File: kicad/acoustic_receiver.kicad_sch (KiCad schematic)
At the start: 17 parts, among them J1 JLI P48 High Z Buffer, J2 Inline Phantom Power 48V, U1 OPA2134, U2 OPA2134, U3 MCP3008

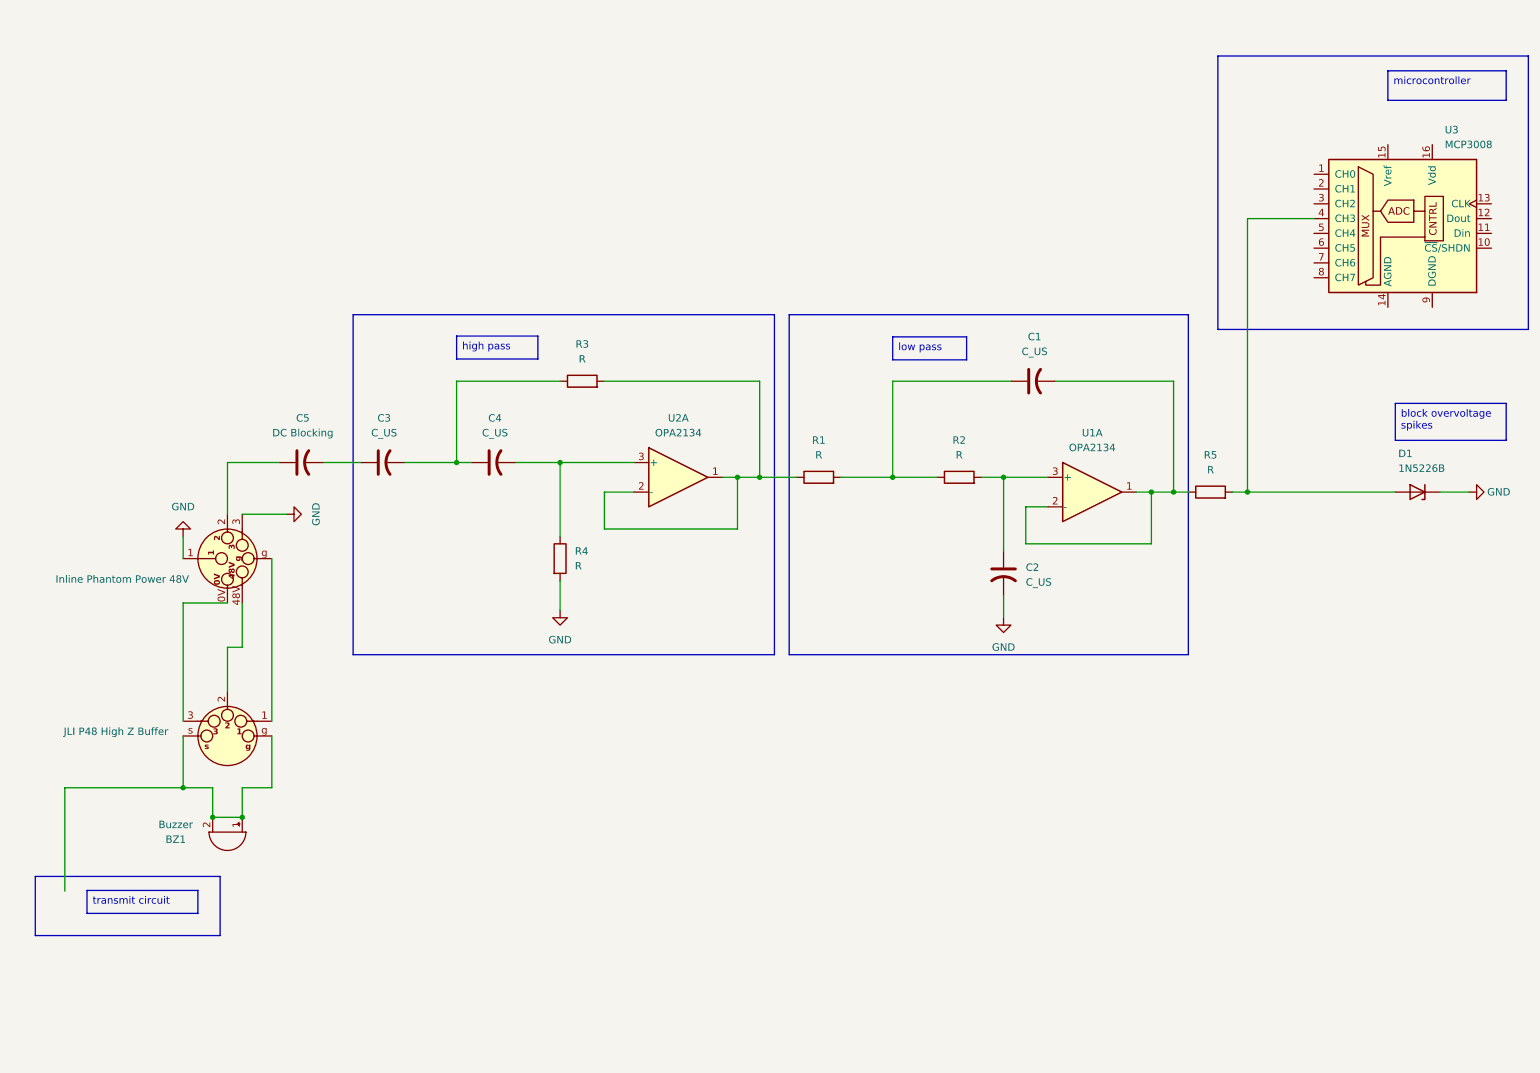
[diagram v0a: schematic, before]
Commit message: update modem diagrams
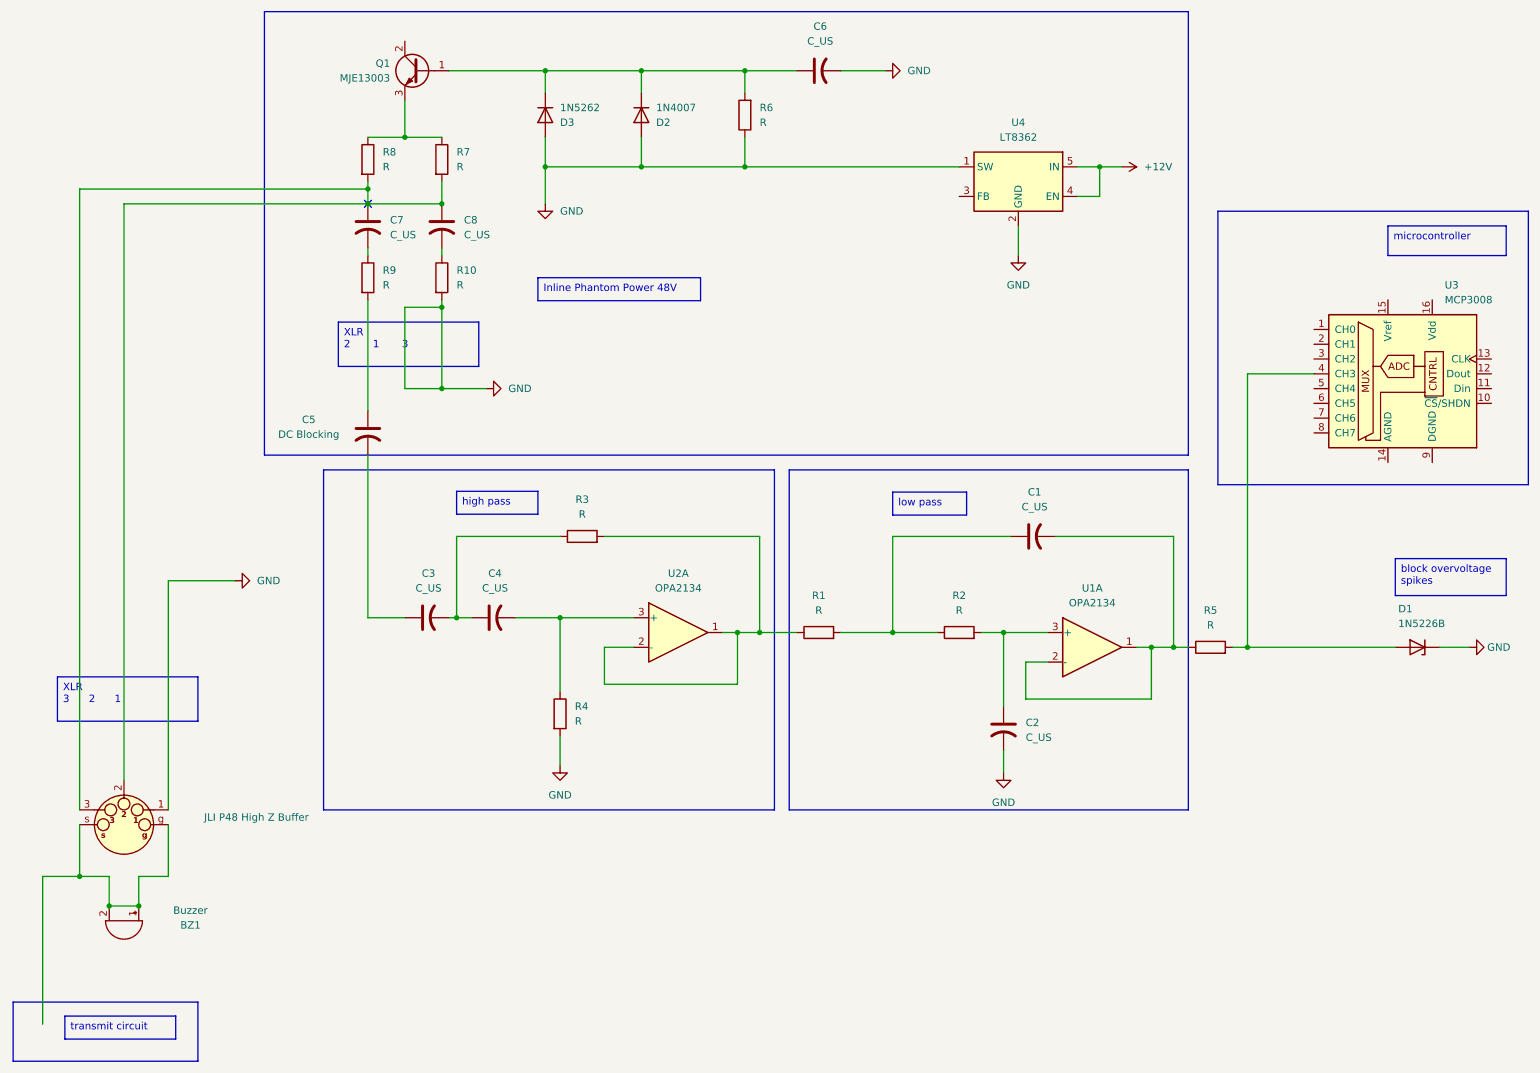
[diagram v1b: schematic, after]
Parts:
- removed J2: Inline Phantom Power 48V, symbol Connector_Audio:XLR6
- added C6, C7, C8: C_US, symbol Device:C_US
- added D2: 1N4007, Diode_THT:D_DO-41_SOD81_P10.16mm_Horizontal, symbol Diode:1N4007
- added D3: 1N5262, Diode_THT:D_DO-41_SOD81_P10.16mm_Horizontal, symbol Diode:1N4007
- added Q1: MJE13003, Package_TO_SOT_THT:TO-126-3_Vertical, symbol Transistor_BJT:MJE13003
- added R10, R6, R7, R8, R9: R, symbol Device:R
- added U4: LT8362, Package_TO_SOT_SMD:SOT-23-5, symbol Regulator_Switching:LGS6302B5
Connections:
- net GND: now also J1.1 (P2), C6.2, D2.2 (A), D3.2 (A), R10.2, R6.1, U4.1 (SW), U4.2 (GND)
- net at J1.2 (P3): now also J1.3 (P3), C7.1, C8.1, R7.2, R8.2
- net at C5.1: now also R9.2
- new net: C6.1, D2.1 (K), D3.1 (K), Q1.1 (B), R6.2
- new net: C8.2, R10.1
- new net: C7.2, R9.1
- new net: Q1.3 (E), R7.1, R8.1
- new net +12V: U4.4 (EN), U4.5 (IN)
- no-connect marks 0 -> 1
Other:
- moved on the sheet: BZ1, C1, C2, C3, C4, C5, D1, R1, R2, R3, R4, R5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

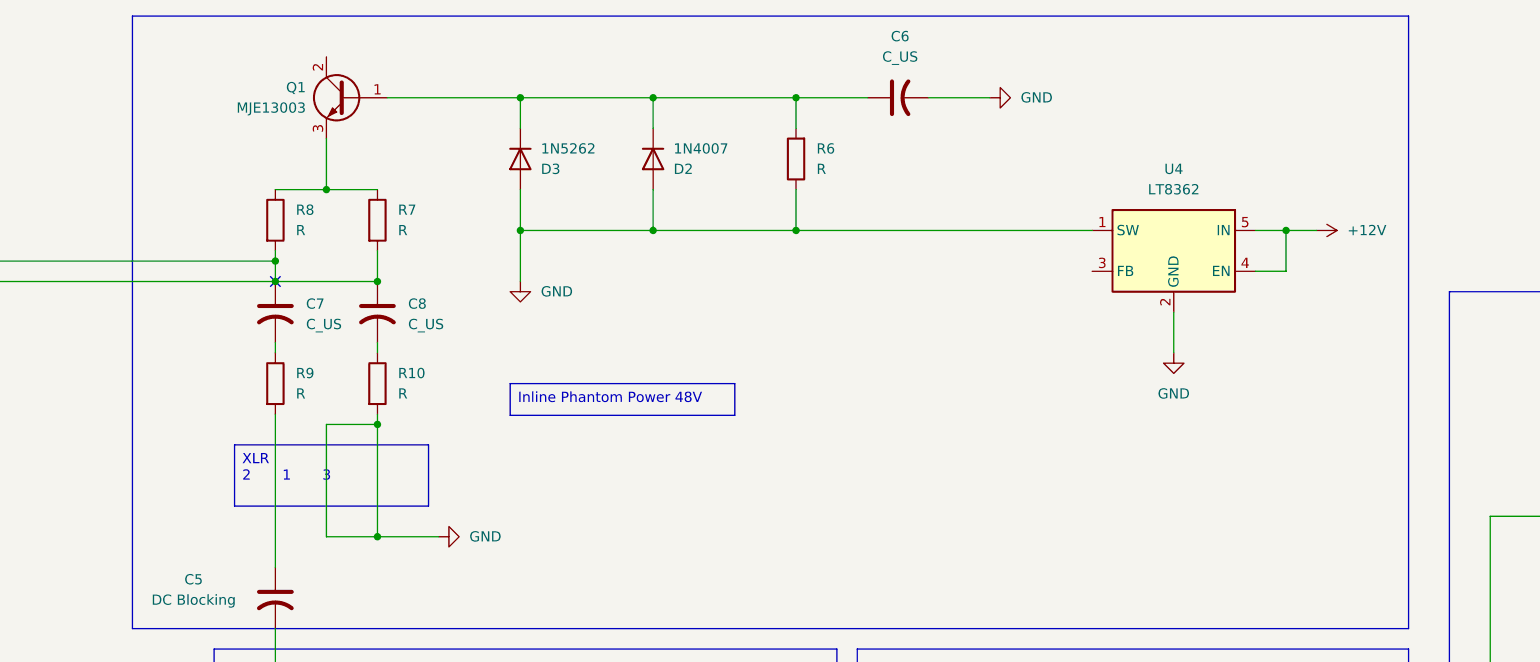
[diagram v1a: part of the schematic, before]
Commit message: FIX 48V phantom power schematic
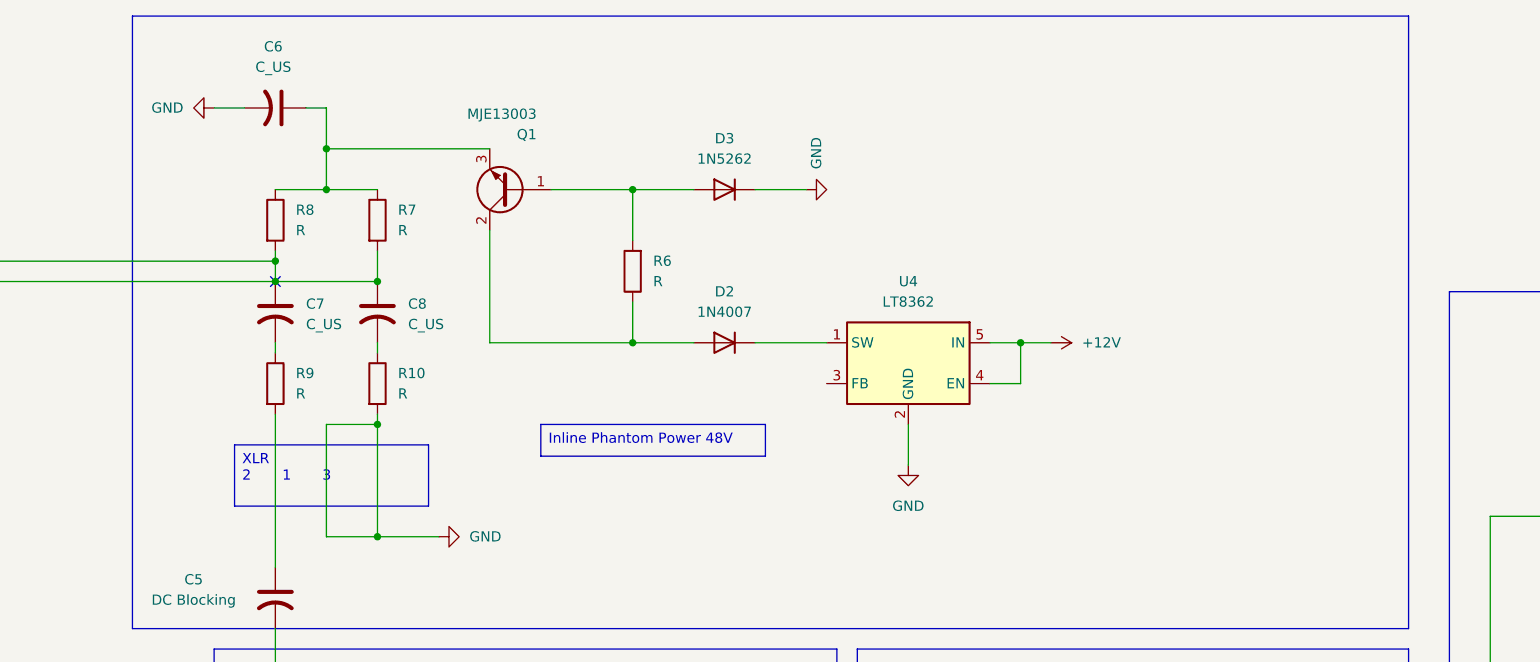
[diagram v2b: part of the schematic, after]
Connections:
- net GND: now also D3.1 (K); no longer D2.2 (A), D3.2 (A), R6.1, U4.1 (SW)
- net at Q1.2 (C): now also D2.2 (A), R6.1
- net at Q1.3 (E), R7.1, R8.1: now also C6.1
- new net: D3.2 (A), Q1.1 (B), R6.2
- new net: D2.1 (K), U4.1 (SW)
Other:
- moved on the sheet: C6, D2, D3, Q1, R6, U4

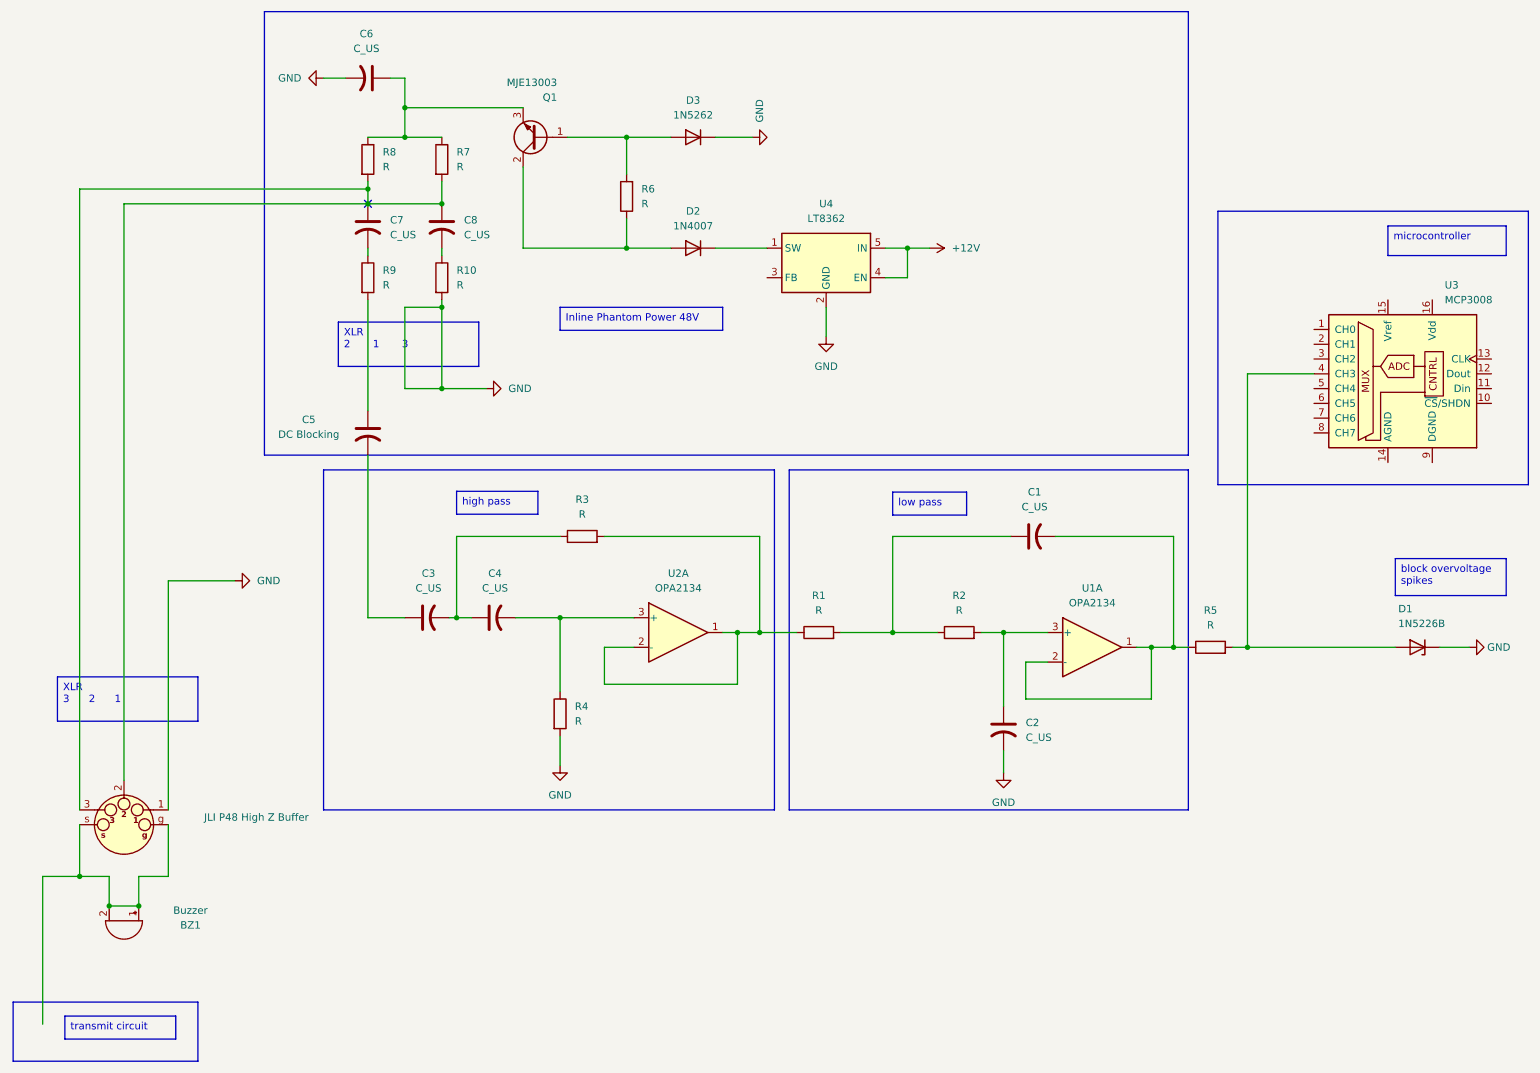
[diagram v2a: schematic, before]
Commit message: add virtual ground and star routing
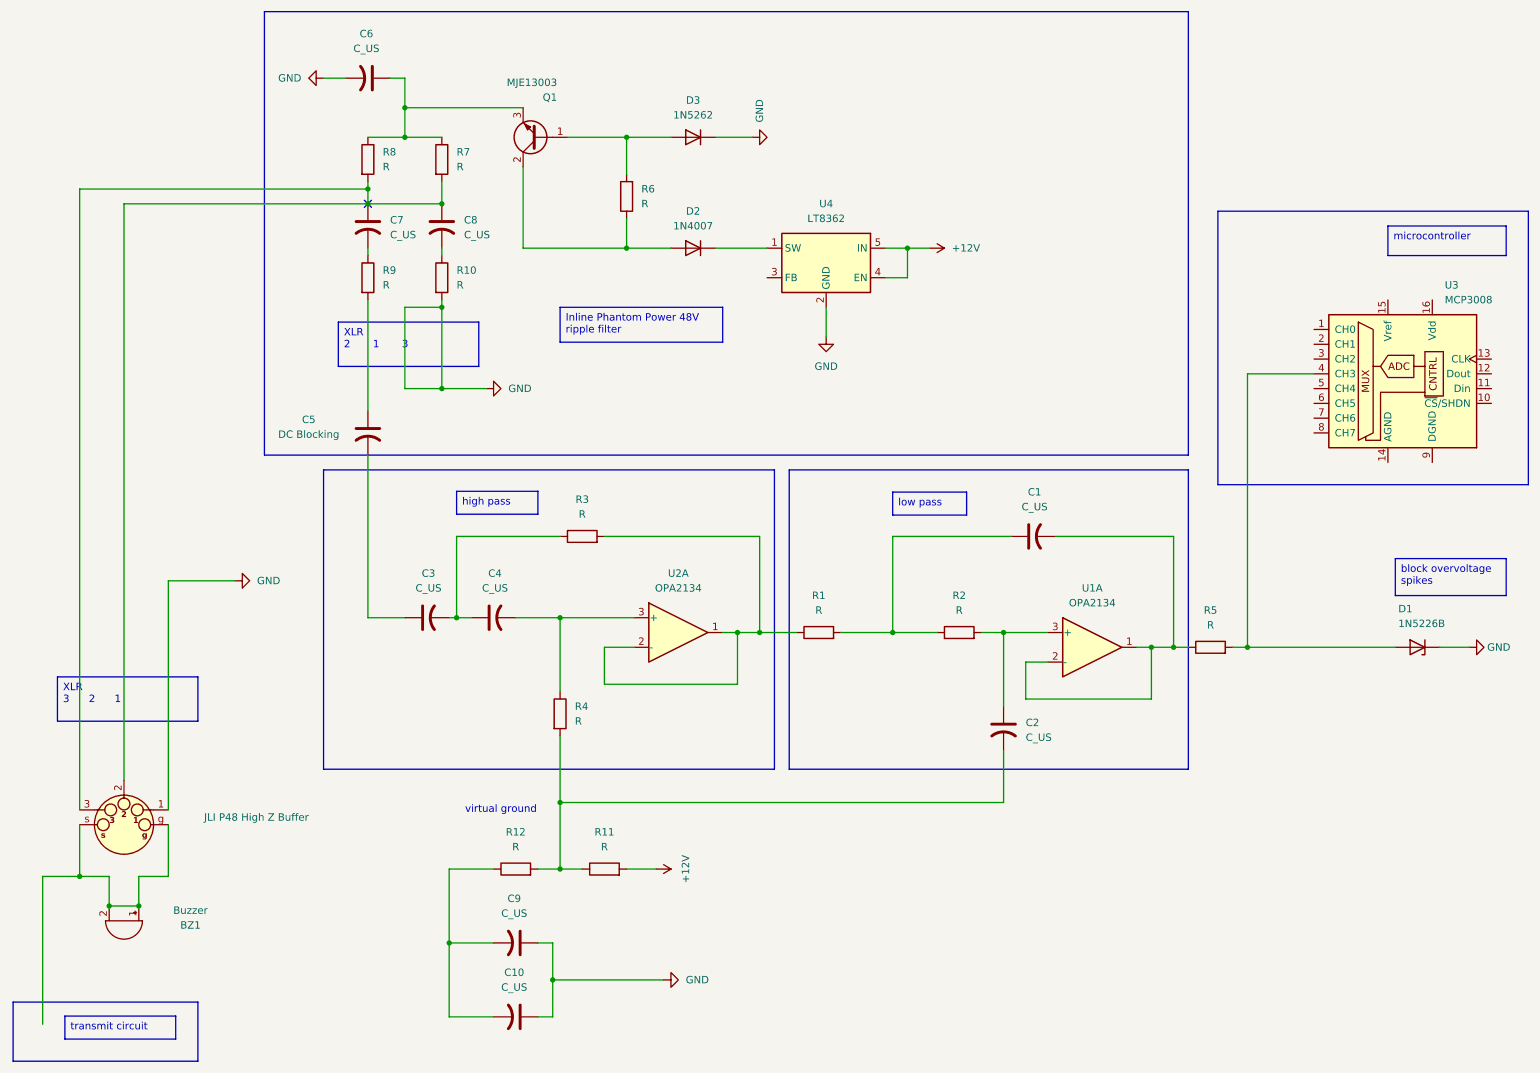
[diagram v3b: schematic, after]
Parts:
- added C10, C9: C_US, symbol Device:C_US
- added R11, R12: R, symbol Device:R
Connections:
- net +12V: now also R11.2
- net GND: now also C10.1, C9.1; no longer C2.2, R4.2
- new net: C10.2, C9.2, R12.1
- new net: C2.2, R11.1, R12.2, R4.2
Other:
- note added: "virtual ground"
